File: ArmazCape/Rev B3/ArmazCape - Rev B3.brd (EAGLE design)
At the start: 85 x 70.5 mm, 167 parts, among them M1 7490100111A, Q1 32.768kHz, 12.5pF, Q2 ASE, Q4 IRLML6344TRPBF, Q5 IRLML6344TRPBF, U1 L7985A, U2 L7985A, U3 DS1307ZN+, U4 24AA256-I/SN, U5 CD4050BD, U6 CD4050BD, U7 PCA9685PW, U8 SN65HVD08D, U9 KSZ8851SNLI

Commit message: Update L7985A FB on ArmazCape - RevB3. sch
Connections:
- removed net N$36: C20.1, R3.2, R4.1
- removed net N$5: C1.2, R1.2, R2.2, U1.5
- new net N$1: C1.2, R1.2, R2.2, R3.2, R4.1, U1.5
- net +12V: now also C20.1
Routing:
- net N$1: track 0.00 -> 7.81 mm, vias 0 -> 1
- net N$5: track 6.28 -> 0.00 mm, vias 1 -> 0
- net N$36: track 3.49 -> 0.00 mm
- net +12V: track 65.8 -> 67.4 mm
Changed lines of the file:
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@@
 </signal>
 <signal name="N$5">
-<contactref element="C1" pad="2"/>
-<contactref element="R2" pad="2"/>
-<contactref element="U1" pad="5"/>
 <polygon width="0.3048" layer="16" thermals="no">
 <vertex x="4.572" y="46.99"/>
@@
 <vertex x="4.572" y="48.514"/>
 </polygon>
-<wire x1="3.7592" y1="46.355" x2="2.921" y2="46.355" width="0.3048" layer="1"/>
-<wire x1="2.921" y1="46.355" x2="2.54" y2="46.736" width="0.3048" layer="1"/>
-<wire x1="2.54" y1="46.736" x2="2.54" y2="48.514" width="0.3048" layer="1"/>
-<wire x1="2.54" y1="48.514" x2="3.048" y2="49.022" width="0.3048" layer="1"/>
-<wire x1="3.048" y1="49.022" x2="3.556" y2="49.022" width="0.3048" layer="1"/>
-<via x="3.556" y="49.022" extent="1-16" drill="0.5"/>
-<wire x1="4.064" y1="48.514" x2="3.556" y2="49.022" width="0.3048" layer="1"/>
-<contactref element="R1" pad="2"/>
-<wire x1="5.246" y1="48.514" x2="4.064" y2="48.514" width="0.3048" layer="1"/>
 </signal>
 <signal name="N$6" class="1">
@@
 <wire x1="23.876" y1="26.416" x2="21.844" y2="26.416" width="0.4064" layer="1"/>
 <via x="21.844" y="26.416" extent="1-16" drill="0.35"/>
+<contactref element="C20" pad="1"/>
+<wire x1="11.596" y1="48.514" x2="9.994" y2="48.514" width="0.3048" layer="1"/>
+<wire x1="28.534" y1="39.116" x2="28.318" y2="42.672" width="0" layer="19" extent="1-1"/>
+<wire x1="25.524" y1="39.37" x2="28.534" y2="39.116" width="0" layer="19" extent="1-1"/>
+<wire x1="22.86" y1="39.37" x2="25.524" y2="39.37" width="0" layer="19" extent="1-1"/>
+<wire x1="22.86" y1="40.64" x2="22.86" y2="39.37" width="0" layer="19" extent="1-1"/>
+<wire x1="22.86" y1="41.91" x2="22.86" y2="40.64" width="0" layer="19" extent="1-1"/>
+<wire x1="22.86" y1="38.1" x2="22.86" y2="39.37" width="0" layer="19" extent="1-1"/>
+<wire x1="22.86" y1="36.83" x2="22.86" y2="38.1" width="0" layer="19" extent="1-1"/>
+<wire x1="24.13" y1="42.802" x2="22.86" y2="41.91" width="0" layer="19" extent="1-1"/>
+<wire x1="20.828" y1="44.45" x2="22.86" y2="41.91" width="0" layer="19" extent="1-1"/>
+<wire x1="11.596" y1="48.514" x2="13.55" y2="48.26" width="0" layer="19" extent="1-1"/>
+<wire x1="23.876" y1="26.416" x2="22.86" y2="36.83" width="0" layer="19" extent="1-1"/>
+<wire x1="28.83" y1="7.23" x2="24.384" y2="25.908" width="0" layer="19" extent="1-1"/>
+<wire x1="29.464" y1="1.27" x2="28.83" y2="2.93" width="0" layer="19" extent="1-16"/>
+<wire x1="28.448" y1="5.08" x2="29.21" y2="5.08" width="0" layer="19" extent="1-1"/>
 </signal>
 <signal name="N$34">
@@
 <contactref element="C20" pad="2"/>
 <wire x1="8.294" y1="48.514" x2="6.946" y2="48.514" width="0.3048" layer="1"/>
-</signal>
-<signal name="N$36">
-<contactref element="R4" pad="1"/>
-<contactref element="R3" pad="2"/>
-<wire x1="11.85" y1="48.26" x2="11.85" y2="46.736" width="0.3048" layer="1"/>
-<contactref element="C20" pad="1"/>
-<wire x1="11.85" y1="48.26" x2="11.596" y2="48.514" width="0.3048" layer="1"/>
-<wire x1="11.596" y1="48.514" x2="9.994" y2="48.514" width="0.3048" layer="1"/>
 </signal>
 <signal name="S$1">
@@
 <wire x1="6.77" y1="57.912" x2="11.85" y2="57.404" width="0" layer="19" extent="1-16"/>
 </signal>
+<signal name="N$1">
+<contactref element="C1" pad="2"/>
+<contactref element="R2" pad="2"/>
+<contactref element="U1" pad="5"/>
+<contactref element="R1" pad="2"/>
+<contactref element="R4" pad="1"/>
+<contactref element="R3" pad="2"/>
+<wire x1="3.7592" y1="46.355" x2="2.921" y2="46.355" width="0.3048" layer="1"/>
+<wire x1="2.921" y1="46.355" x2="2.54" y2="46.736" width="0.3048" layer="1"/>
+<wire x1="2.54" y1="46.736" x2="2.54" y2="48.514" width="0.3048" layer="1"/>
+<wire x1="2.54" y1="48.514" x2="3.048" y2="49.022" width="0.3048" layer="1"/>
+<wire x1="3.048" y1="49.022" x2="3.556" y2="49.022" width="0.3048" layer="1"/>
+<via x="3.556" y="49.022" extent="1-16" drill="0.5"/>
+<wire x1="4.064" y1="48.514" x2="3.556" y2="49.022" width="0.3048" layer="1"/>
+<wire x1="5.246" y1="48.514" x2="4.064" y2="48.514" width="0.3048" layer="1"/>
+<wire x1="11.85" y1="48.26" x2="11.85" y2="46.736" width="0.3048" layer="1"/>
+<wire x1="6.77" y1="49.022" x2="11.85" y2="48.26" width="0" layer="19" extent="1-16"/>
+<wire x1="5.246" y1="48.514" x2="6.77" y2="49.022" width="0" layer="19" extent="1-16"/>
+<wire x1="3.722" y1="47.752" x2="4.064" y2="48.514" width="0" layer="19" extent="1-16"/>
+</signal>
 </signals>

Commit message: Added GERBER RS274X files for Varmo - Rev A1
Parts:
- moved D3 17.3 mm to (14.0, 34.9), turned to 270 degrees
- moved D4 17.0 mm to (14.0, 55.9), turned to 90 degrees
- moved 12V 12.1 mm to (31.8, 35.6)
- moved C12 7.87 mm to (31.1, 47.6), turned to 270 degrees
- moved R33 4.30 mm to (10.3, 59.4), turned to 270 degrees
- moved R34 4.07 mm to (8.64, 57.7), turned to 270 degrees
- moved U$1 3.59 mm to (38.4, 41.7)
- moved R52 3.03 mm to (22.9, 26.0)
- moved L1 2.37 mm to (22.9, 38.7)
- moved L4 2.32 mm to (22.9, 51.4)
- moved 5V 2.09 mm to (31.8, 54.6)
- moved C19 2.05 mm to (7.11, 57.7), turned to 90 degrees
- moved C3 1.40 mm to (31.1, 42.5), turned to 90 degrees
- moved R11 0.57 mm to (5.59, 57.7), turned to 270 degrees
- moved R36 0.51 mm to (41.7, 23.9)
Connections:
- removed net N$31: OK2.3, R36.2
- removed net N$6: L1.1, U1.1
- new net N$30: D3.C, L1.1, U1.1
- new net N$5: OK2.2, R36.2
- net +12V: no longer D3.C
- net +5V: no longer D4.C
- net +5V/1: no longer OK2.2
- net GND1: now also OK2.3
- net N$19: now also D4.C
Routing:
- net GND1: track 64.0 -> 72.4 mm
- net N$1: track 7.81 -> 14.6 mm, vias 1 -> 2
- net N$21: track 7.81 -> 14.2 mm
- net N$5: track 0.00 -> 6.33 mm
- net +5V: track 28.6 -> 34.4 mm
- net +12V: track 67.4 -> 72.2 mm, vias 10 -> 9
- net N$31: track 4.27 -> 0.00 mm
- net DV0: track 92.0 -> 87.8 mm
- net +5V/1: track 21.3 -> 19.2 mm
- net VBAT+: track 72.9 -> 72.0 mm
- net N$53: track 1.66 -> 2.55 mm
- net +3V3: track 139.3 -> 138.6 mm, vias 19 -> 18
- net N$27: track 1.75 -> 2.26 mm
- net GND: vias 61 -> 57
- added copper zone on layer 16, net N$1
- added copper zone on layer 1, net N$30
- removed copper zone on layer 16, net N$5
- removed copper zone on layer 1, net N$6
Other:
- board text added: "ArmazCape Rev B3"
- board text removed: "ArmazCape Rev B2"

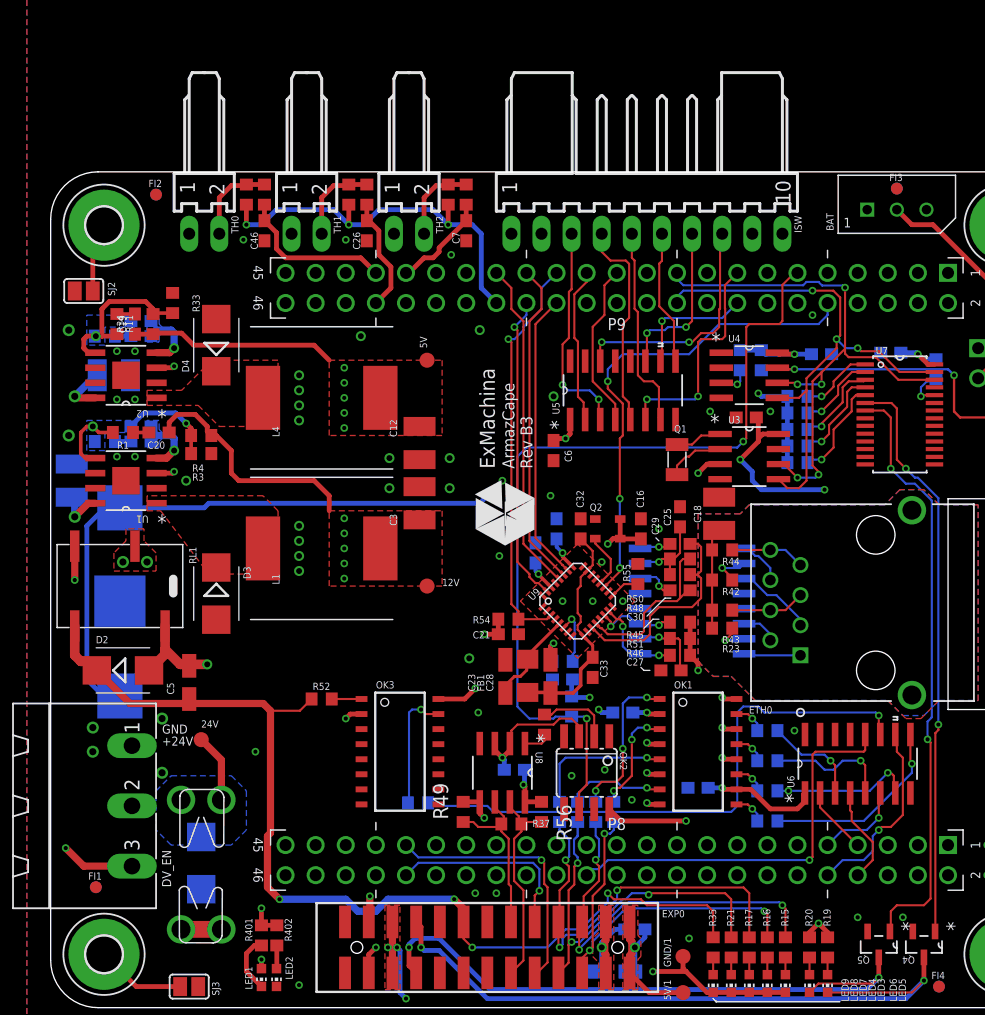
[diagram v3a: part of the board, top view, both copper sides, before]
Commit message: ArmazCape - Rev B3 updated:
Fix for +5V and +12V power chips
Routed KSZ8851SNL according to Evaluation-board schematics
Modified 7490100111A symbol to avoid future mistakes
Moved KSZ8851SNL RSTN to P9.12 instead of SYS_RESET
Moved SW_0 to P9.14 (pin conflict)
Added pulldown on all buffer inputs
TLP283 output +5V to trigger input buffer
Added pulldown on SN65HVD08D on R pin

Reduced fuse holder spacing
Reduced width on keystone 3000 footprint
Moved CC-BY-SA to tPlace layer
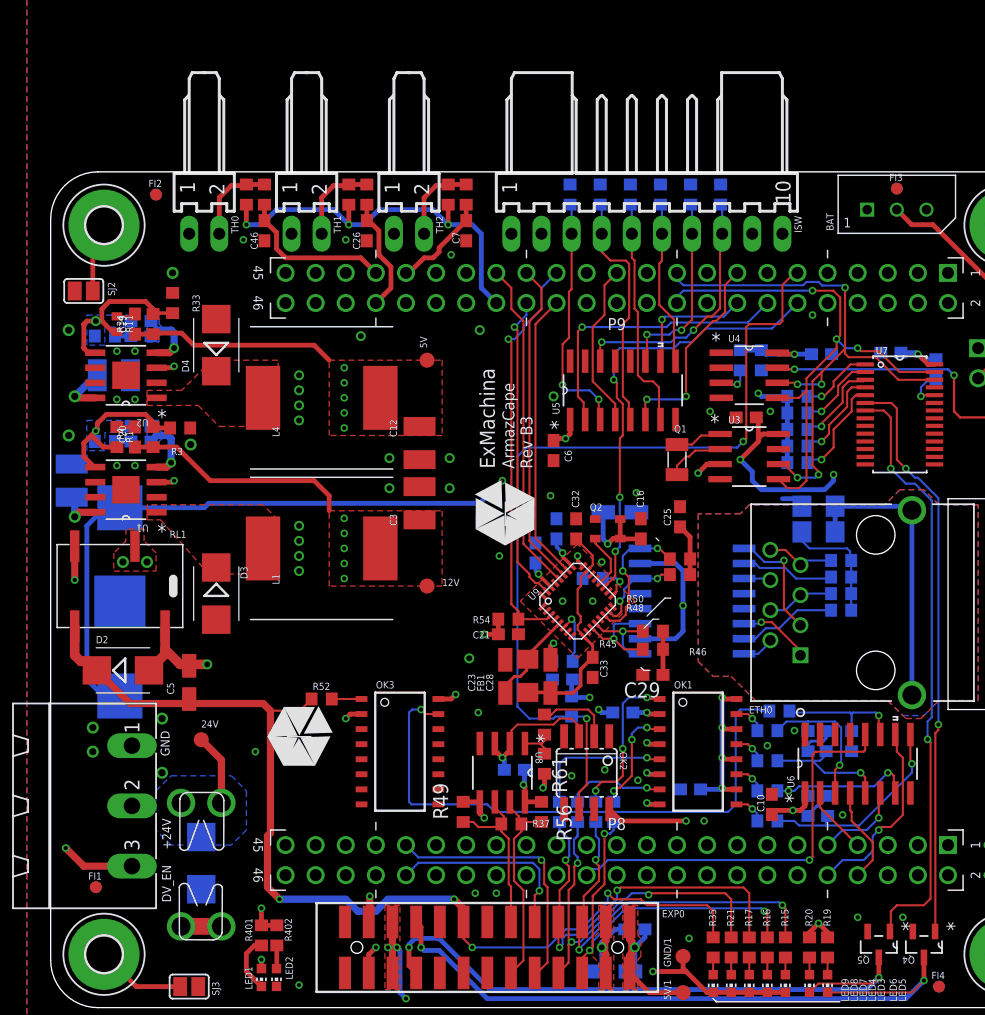
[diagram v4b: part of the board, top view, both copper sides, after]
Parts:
- added C37: 1000pF, 2kV, rcl:C1206
- added R57, R58, R59, R60, R61, R62, R63, R64, R65, R66, R67: 3K3, rcl:R0603
- added U$5: (no value), exmachina:EXM-LOGO-BIG
- C18: device rcl:C1210 -> rcl:C1206
- C27: value 0.01uF -> 0.1uF
- C29: value 6.8nF -> 0.01uF
- C30: value 6.8nF -> 4.7uF; device rcl:C0603 -> rcl:CT3216
- R11: device rcl:R0603 -> rcl:R0402
- R51: value 10 -> 3K3
- moved U$3 192.5 mm to (87.8, 32.6), flipped to the bottom
- moved R53 31.4 mm to (61.5, 25.0)
- moved R51 13.8 mm to (63.9, 22.5), flipped to the bottom, turned to 270 degrees
- moved C29 11.3 mm to (50.8, 28.1)
- moved R23 10.9 mm to (66.7, 36.3), flipped to the bottom
- moved R42 10.3 mm to (66.7, 33.5), flipped to the bottom
- moved C27 10.2 mm to (54.0, 18.4), flipped to the bottom, turned to 0 degrees
- moved R43 10.1 mm to (66.7, 34.9), flipped to the bottom
- moved R44 10.1 mm to (66.7, 37.7), flipped to the bottom
- moved C18 8.52 mm to (64.8, 40.1), flipped to the bottom, turned to 180 degrees
- moved C30 8.31 mm to (48.0, 41.8), flipped to the bottom
- moved C10 6.38 mm to (60.8, 17.1), flipped to the top, turned to 90 degrees
- moved R4 4.07 mm to (8.64, 48.1), turned to 270 degrees
- moved R55 3.83 mm to (45.7, 36.2), flipped to the bottom, turned to 0 degrees
- moved R3 2.80 mm to (10.9, 48.9)
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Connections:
- net SPI1_INT renamed !KSZ8851_INT
- removed net N$2000: C29.1, R48.2, U9.11
- removed net N$300: C30.1, R50.2, U9.12
- removed net N$4200: M1.3, R45.2, U9.14
- removed net N$4400: M1.1, R46.1, U9.15
- removed net N$50: C25.1, M1.7, R48.1, R50.1
- removed net N$51: C29.2, M1.8
- removed net SW_EXT5: U6.15
- removed net SW_EXT5_IN: U6.14
- new net !KSZ8851_RST: BB1.P9.12, U9.19
- new net GNDI: C18.2, C37.2, ETH0.M1, ETH0.M2
- new net N$31: M1.1, R45.2, U9.12
- new net N$36: M1.8, R50.1, U9.14
- new net N$37: M1.6, R48.1, U9.15
- new net N$6: ETH0.6, M1.11
- net +3V3: now also C30.+, M1.2, M1.7; no longer OK1.10, OK1.12, OK1.14, OK1.16, OK3.16, R45.1, R46.2, R51.1
- net +5V: now also C27.1, OK1.10, OK1.12, OK1.14, OK1.16, OK3.16
- net GND: now also C29.2, C30.-, C37.1, R51.2, R57.2, R58.2, R59.2, R60.2, R62.2, R63.2, R64.2, R65.2, R66.2, R67.2; no longer C18.2
- net GND1: now also R61.2
- net N$27: now also R61.1
- net N$4: now also M1.3, R46.2, U9.11; no longer C30.2, M1.6
- net N$40: now also M1.14; no longer M1.16
- net N$41: now also M1.16; no longer M1.14
- net N$42: now also M1.9; no longer M1.11
- net N$43: now also C25.1, R48.2, R50.2; no longer ETH0.6, M1.9
- net N$44: now also M1.10; no longer M1.15
- net N$45: now also M1.15; no longer M1.10
- net N$49: now also C29.1, R45.1, R46.1; no longer C27.1, M1.2, R51.2
- net SW_0: now also BB1.P9.14; no longer BB1.P9.25
- net SW_0_IN: now also R62.1
- net SW_1_IN: now also R63.1
- net SW_2_IN: now also R64.1
- net SW_3_IN: now also R65.1
- net SW_4_IN: now also R66.1
- net SW_5_IN: now also R67.1
- net SW_EXT0_IN: now also R51.1
- net SW_EXT1_IN: now also R57.1
- net SW_EXT2_IN: now also R58.1
- net SW_EXT3_IN: now also R59.1
- net SW_EXT4_IN: now also R60.1
- net SYS_RESET: no longer U9.19
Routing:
- net SYS_RESET: track 41.0 -> 0.00 mm, vias 3 -> 0
- net N$54: track 10.4 -> 49.1 mm
- net !KSZ8851_RST: track 0.00 -> 37.9 mm, vias 0 -> 3
- net SW_EXT4_IN: track 48.6 -> 10.9 mm
- net GNDI: track 0.00 -> 24.4 mm
- net N$2000: track 18.3 -> 0.00 mm
- net +5V: track 34.4 -> 52.1 mm, vias 8 -> 13
- net N$300: track 14.8 -> 0.00 mm
- net N$36: track 0.00 -> 12.1 mm, vias 0 -> 2
- net SW_0: track 13.2 -> 24.7 mm, vias 0 -> 1
- net GND: track 1.50 -> 9.86 mm, vias 57 -> 61
- net N$4400: track 7.94 -> 0.00 mm, vias 2 -> 0
- net N$37: track 0.00 -> 7.91 mm, vias 0 -> 2
- net N$50: track 7.26 -> 0.00 mm, vias 1 -> 0
- net N$31: track 0.00 -> 7.24 mm, vias 0 -> 1
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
